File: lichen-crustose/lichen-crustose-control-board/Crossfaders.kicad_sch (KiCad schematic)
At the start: 20 parts

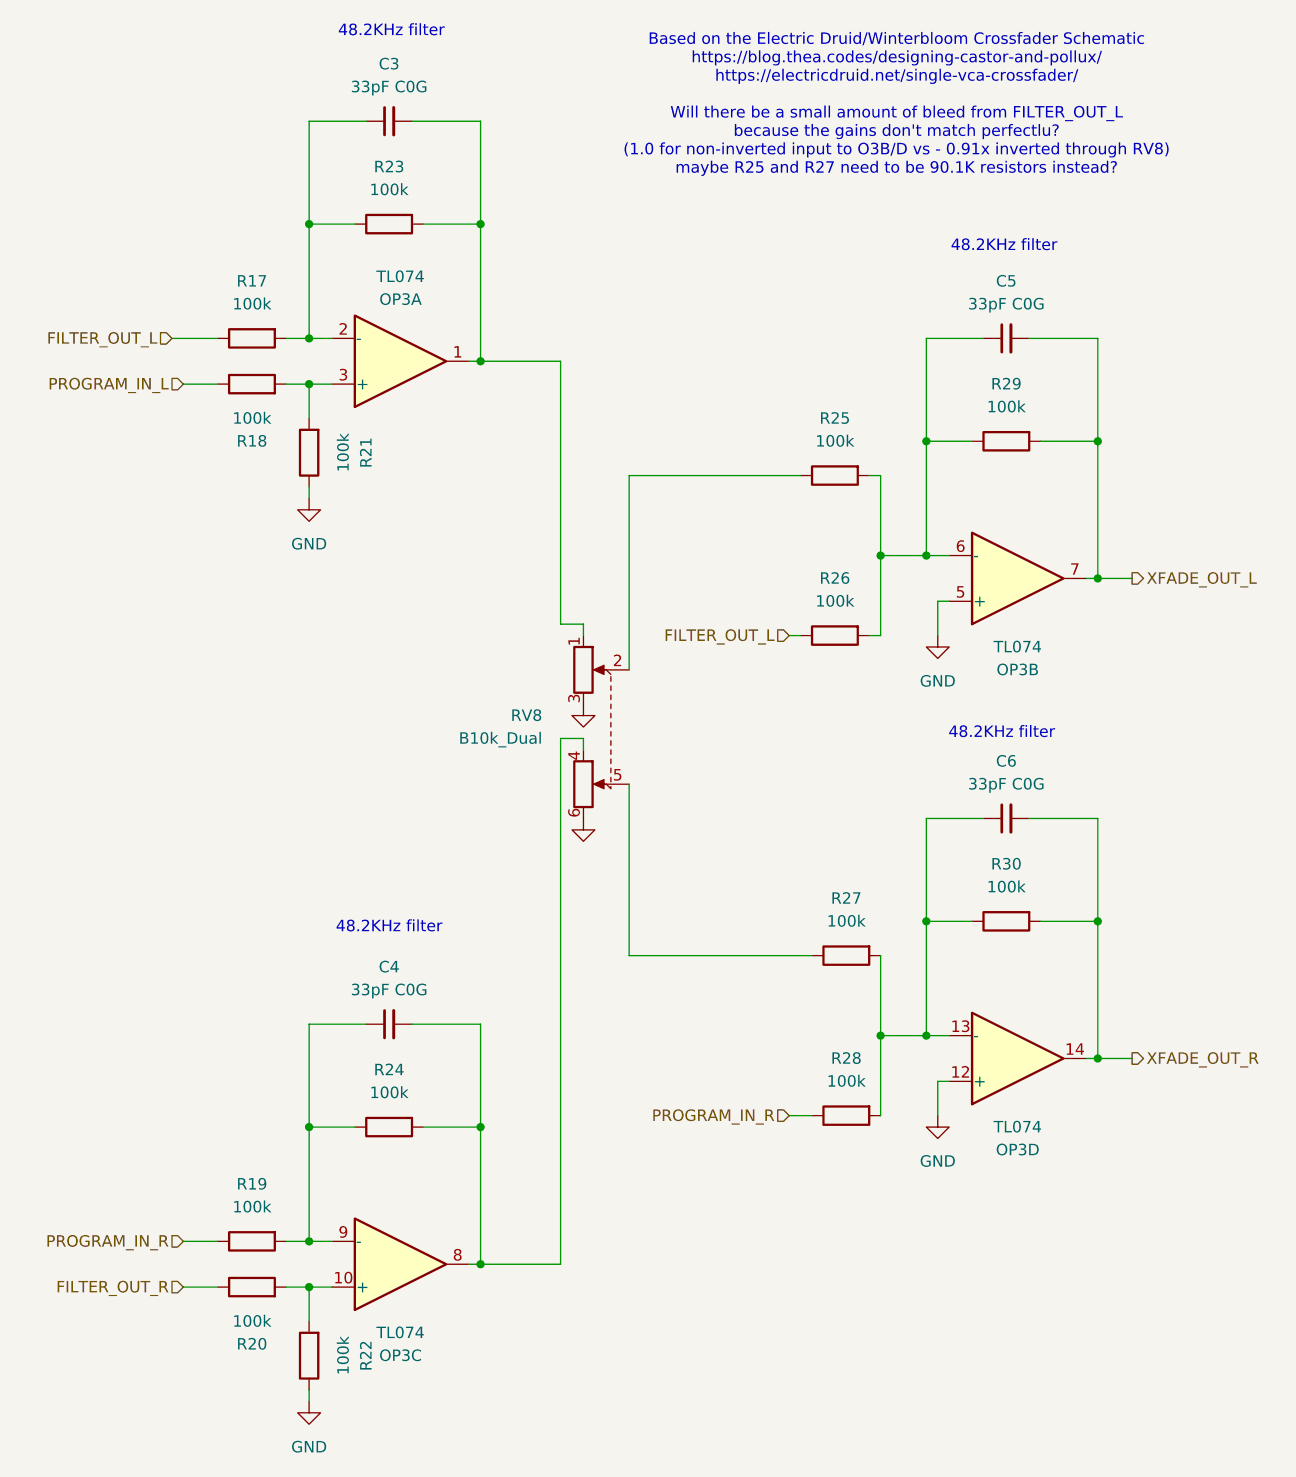
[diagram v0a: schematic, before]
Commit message: Updates Lichen symbols and footprints. Fixes to Crustose and Vactrol VCA. Adds 3D model of the RP2350 dual USB board.
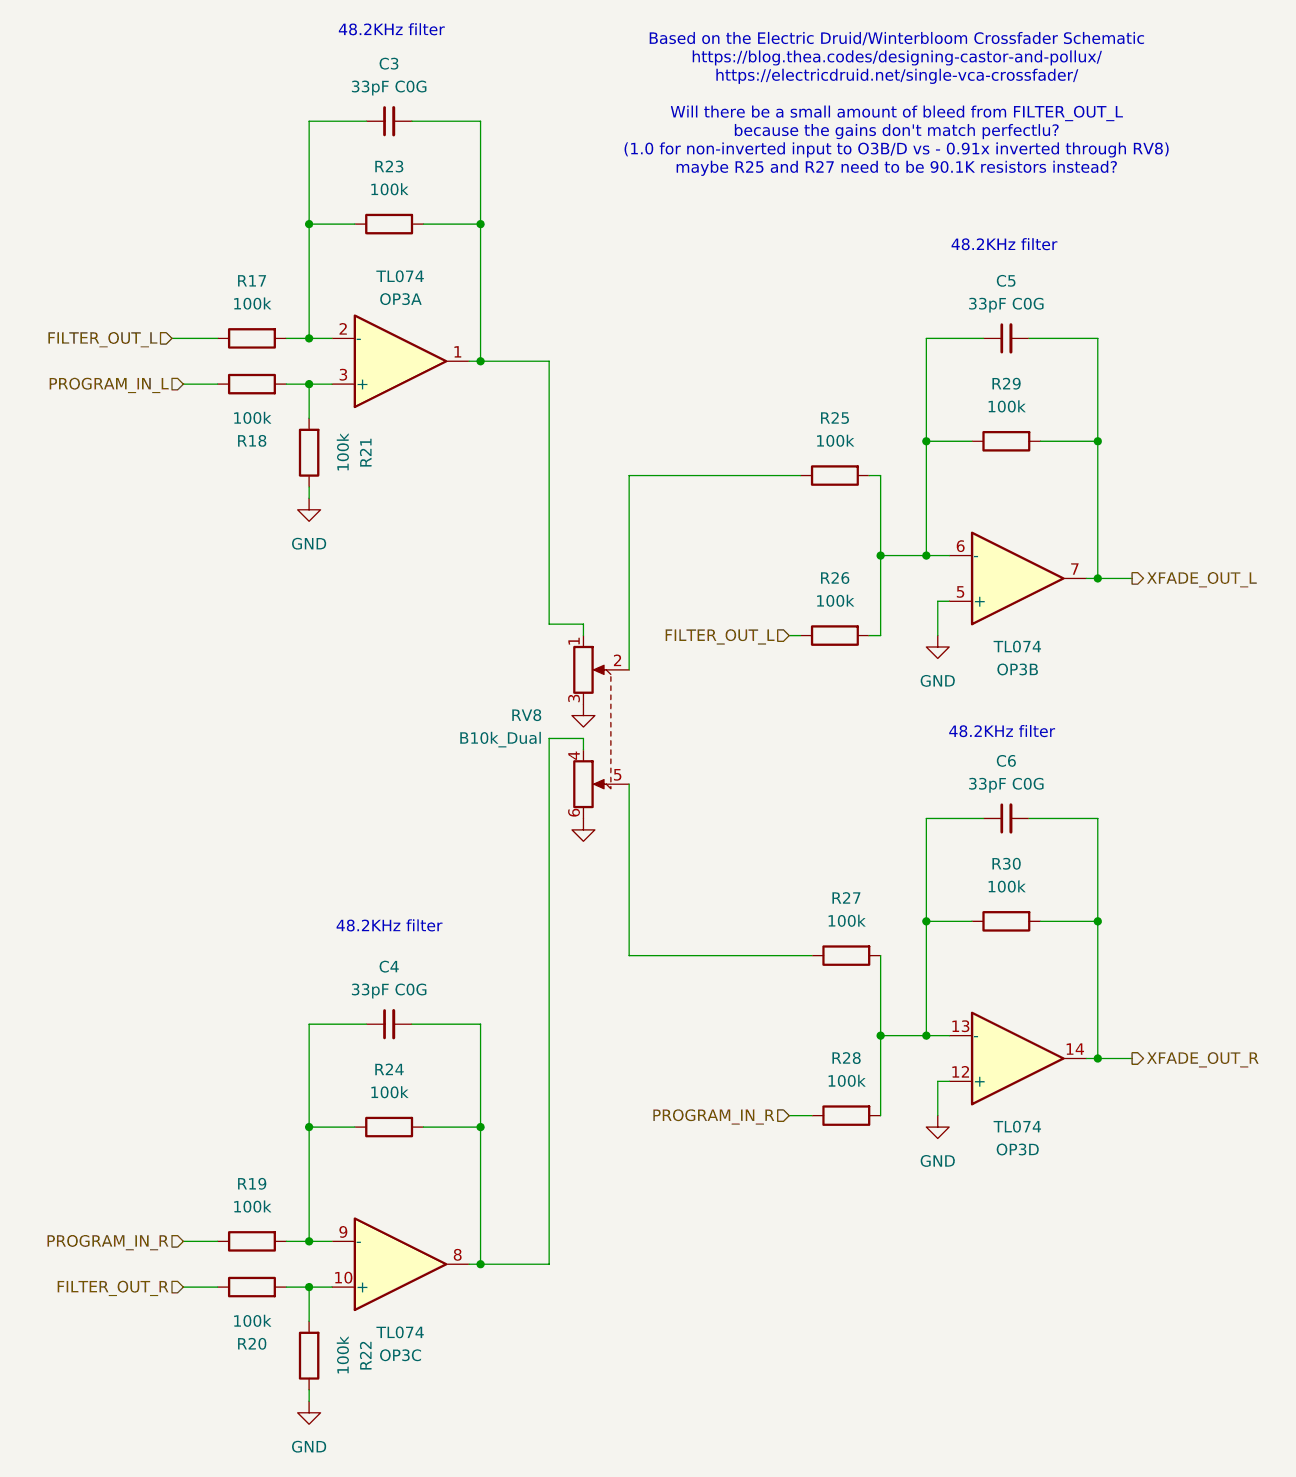
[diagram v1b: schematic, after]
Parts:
- R17, R18, R19, R20, R21, R22, R23, R24, R25, R26, R27, R28, R29, R30: JLCPCB ID C25803 -> (none); LCSC (none) -> C25803
- RV8: now left out of the parts list
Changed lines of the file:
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@@
 	(wire
 		(pts
-			(xy 87.63 162.56) (xy 96.52 162.56)
+			(xy 87.63 162.56) (xy 95.25 162.56)
 		)
 		(stroke
@@
 	(wire
 		(pts
-			(xy 96.52 62.23) (xy 96.52 91.44)
+			(xy 95.25 62.23) (xy 95.25 91.44)
 		)
 		(stroke
@@
 	(wire
 		(pts
-			(xy 96.52 104.14) (xy 99.06 104.14)
+			(xy 95.25 104.14) (xy 99.06 104.14)
 		)
 		(stroke
@@
 	(wire
 		(pts
-			(xy 96.52 104.14) (xy 96.52 162.56)
+			(xy 95.25 104.14) (xy 95.25 162.56)
 		)
 		(stroke
@@
 	(wire
 		(pts
-			(xy 96.52 91.44) (xy 99.06 91.44)
+			(xy 95.25 91.44) (xy 99.06 91.44)
 		)
 		(stroke
@@
 	(wire
 		(pts
-			(xy 87.63 62.23) (xy 96.52 62.23)
+			(xy 87.63 62.23) (xy 95.25 62.23)
 		)
 		(stroke
@@
 			)
 		)
-		(property "JLCPCB ID" "C25803"
+		(property "LCSC" "C25803"
 			(at 92.71 48.26 0)
 			(effects
@@
 			)
 		)
-		(property "JLCPCB ID" "C25803"
+		(property "LCSC" "C25803"
 			(at 77.47 60.96 0)
 			(effects
@@
 			)
 		)
-		(property "JLCPCB ID" "C25803"
+		(property "LCSC" "C25803"
 			(at 92.71 148.59 0)
 			(effects
@@
 			)
 		)
-		(property "JLCPCB ID" "C25803"
+		(property "LCSC" "C25803"
 			(at 77.47 163.83 0)
 			(effects
@@
 			)
 		)
-		(property "JLCPCB ID" "C25803"
+		(property "LCSC" "C25803"
 			(at 161.29 125.73 0)
 			(effects
@@
 			)
 		)
-		(property "JLCPCB ID" "C25803"
+		(property "LCSC" "C25803"
 			(at 77.47 161.29 0)
 			(effects
@@
 			)
 		)
-		(property "JLCPCB ID" "C25803"
+		(property "LCSC" "C25803"
 			(at 161.29 72.39 0)
 			(effects
@@
 			)
 		)
-		(property "JLCPCB ID" "C25803"
+		(property "LCSC" "C25803"
 			(at 77.47 63.5 0)
 			(effects
@@
 			)
 		)
-		(property "JLCPCB ID" "C25803"
+		(property "LCSC" "C25803"
 			(at 67.31 57.15 0)
 			(effects
@@
 			)
 		)
-		(property "JLCPCB ID" "C25803"
+		(property "LCSC" "C25803"
 			(at 67.31 157.48 0)
 			(effects
@@
 			)
 		)
-		(property "JLCPCB ID" "C25803"
+		(property "LCSC" "C25803"
 			(at 142.24 76.2 0)
 			(effects
@@
 			)
 		)
-		(property "JLCPCB ID" "C25803"
+		(property "LCSC" "C25803"
 			(at 142.24 93.98 0)
 			(effects
@@
 			)
 		)
-		(property "JLCPCB ID" "C25803"
+		(property "LCSC" "C25803"
 			(at 143.51 147.32 0)
 			(effects
@@
 		(unit 1)
 		(exclude_from_sim no)
-		(in_bom yes)
+		(in_bom no)
 		(on_board yes)
 		(dnp no)
@@
 			)
 		)
-		(property "JLCPCB ID" "C25803"
+		(property "LCSC" "C25803"
 			(at 143.51 129.54 0)
 			(effects

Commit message: feat: Updates Crustose, Cladonia and YouMe Transformer. Adds Stereo Latencies.
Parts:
- C3, C4, C5, C6: value 33pF_C0G_0603_50V -> 33pF C0G; Specifications 33pF 50V C0G ±5% 0603 MLCC -> (none)
- OP3: symbol Amplifier_Operational:TL074 -> Lichen:TL074; LCSC (none) -> C6964; Manufacturer (none) -> Texas Instruments; Part Number (none) -> TL074IDR
- R17, R18, R19, R20, R21, R22, R23, R24, R25, R26, R27, R28, R29, R30: value 100k_0603 -> 100K
- RV8: value B10k_Dual -> B10K; symbol Lichen:10K_Potentiometer_Dual_Gang_Alpha_RD902F -> Lichen:R_Potentiometer_Dual
